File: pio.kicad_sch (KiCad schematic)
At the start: 9 parts, among them J1 PIO, Q1 2N7002

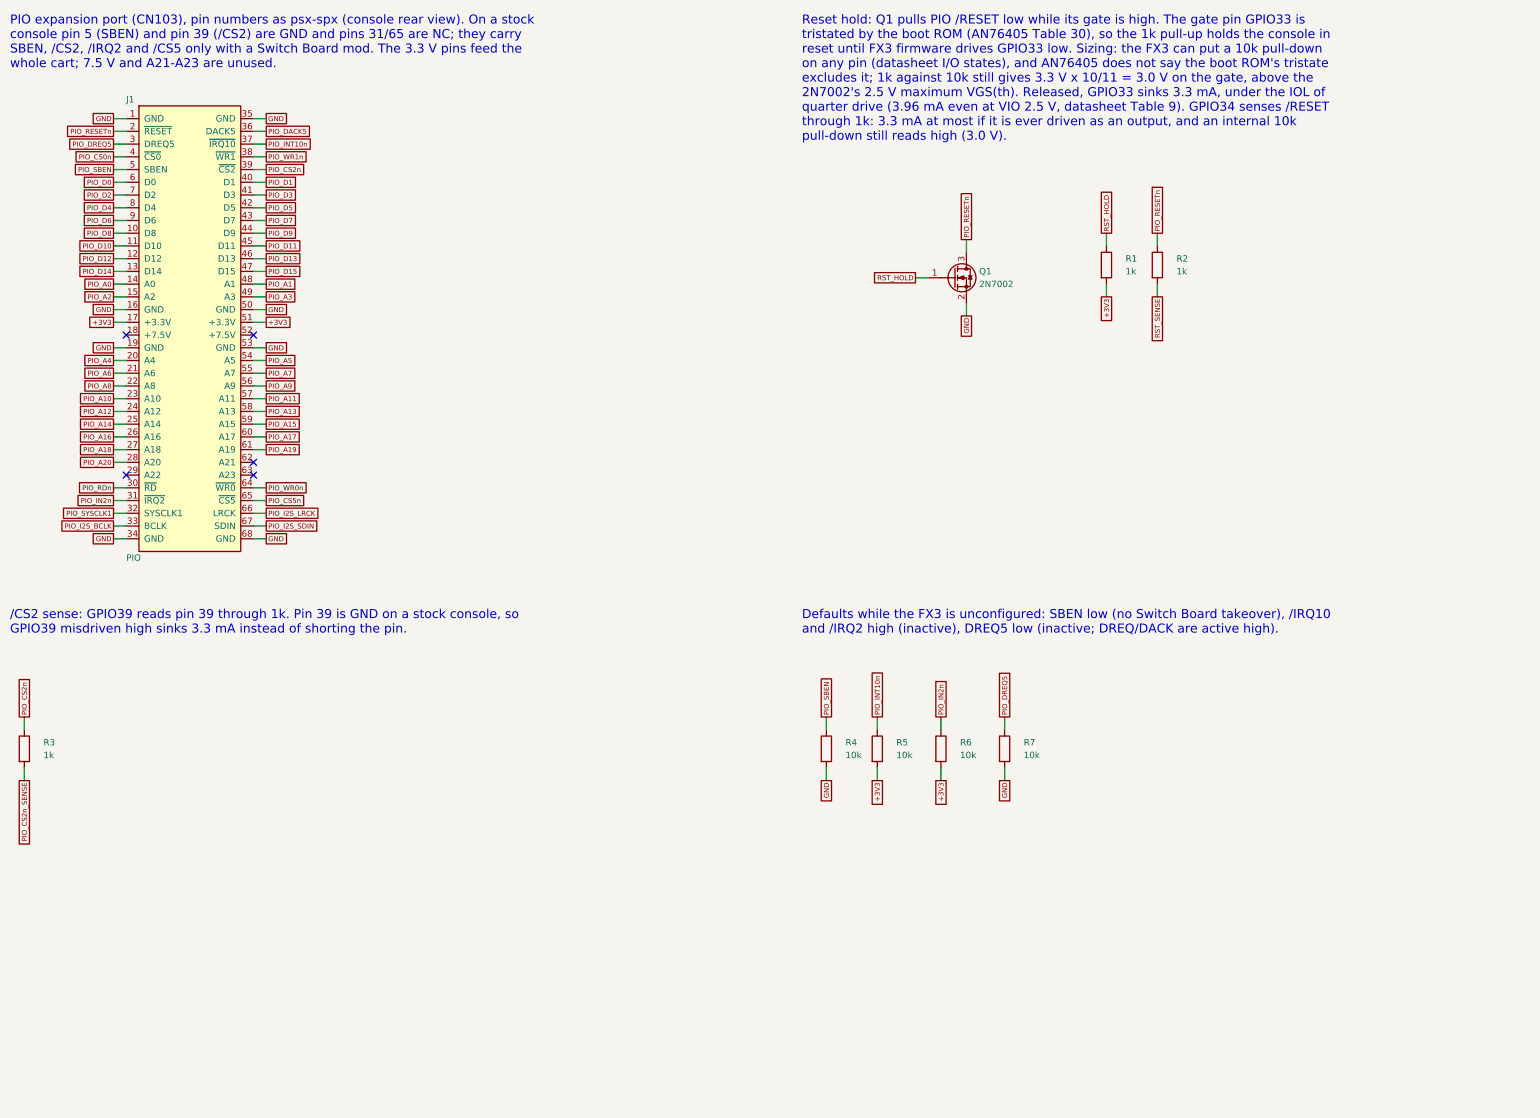
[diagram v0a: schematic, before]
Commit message: PIO sheet: GPIO37 drives SBEN through 1k
Pin 5 is GND on a stock console, so a GPIO37 driven high sinks 3.3 mA
instead of shorting it. check_netlist checks the hop like /RESET and /CS2.
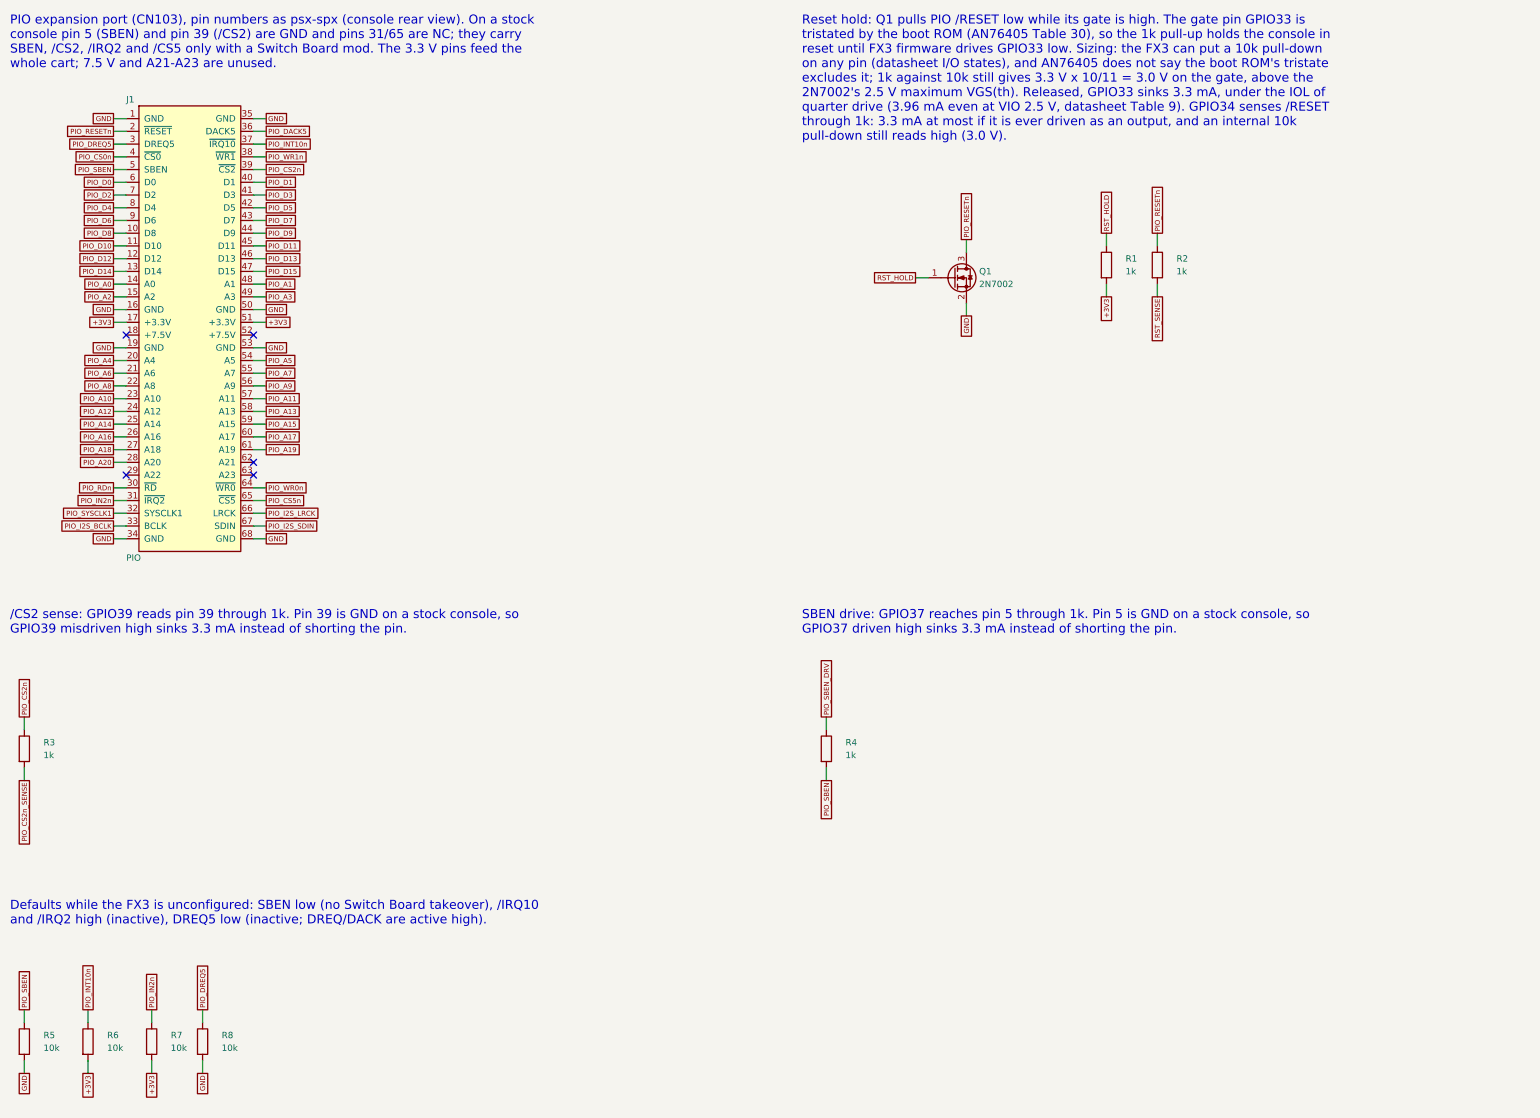
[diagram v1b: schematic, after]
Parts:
- added R8: 10k, Resistor_SMD:R_0402_1005Metric, symbol Device:R
- R4: value 10k -> 1k; LCSC C25744 -> C11702
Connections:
- net +3V3: now also R7.2; no longer R5.2
- net GND: now also R5.2, R8.2; no longer R4.2, R7.2
- net PIO_DREQ5: now also R8.1; no longer R7.1
- net PIO_IN2n: now also R7.1; no longer R6.1
- net PIO_INT10n: now also R6.1; no longer R5.1
- net PIO_SBEN: now also R4.2, R5.1; no longer R4.1
- new net PIO_SBEN_DRV: R4.1
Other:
- note added: "SBEN drive: GPIO37 reaches pin 5 through 1k. Pin 5 is GND on a stock console, so GPIO37 driven high sinks 3.3 mA instead of shorting the pin."
